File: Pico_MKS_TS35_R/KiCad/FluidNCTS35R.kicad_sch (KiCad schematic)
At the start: 8 parts, among them J1 Conn_01x03_Pin, J2 Conn_01x03_Pin, U1 Pico

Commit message: Add PCB
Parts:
- added C1, C2, C3: C_Polarized, Capacitor_SMD:C_1210_3225Metric_Pad1.33x2.70mm_HandSolder, symbol Device:C_Polarized
- J1: footprint Connector_JST:JST_SH_SM03B-SRSS-TB_1x03-1MP_P1.00mm_Horizontal -> Connector_PinSocket_2.54mm:PinSocket_1x03_P2.54mm_Horizontal
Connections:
- net +3V3: now also C1.1
- net +5V: now also C3.1
- net GND: now also C1.2, C2.2, C3.2
- net VDD: now reaches D1.1 (K), U1.39 (VSYS)
- net VDD: now also C2.1
- net SWCLK: now reaches J1.1 (Pin_1), U1.41 (SWCLK)
- net SWDIO: now reaches J1.3 (Pin_3), U1.43 (SWDIO)

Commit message: Add PCB and some button handlers
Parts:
- added TP1, TP10, TP11, TP12, TP13, TP14, TP15, TP16, TP2, TP3, TP4, TP5, TP6, TP7, TP8, TP9: TestPoint, TestPoint:TestPoint_Pad_D2.0mm, symbol Connector:TestPoint
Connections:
- net +3V3: now also TP12.1
- net +5V: now also TP14.1
- net BEEPER: now also TP6.1
- net GND: now also J2.2 (Pin_2), TP11.1, TP15.1, TP16.1; no longer J2.3 (Pin_3)
- net LCD_BACKLIGHT: now also TP7.1
- net LCD_CS: now also TP9.1
- net LCD_RESET: now also TP5.1
- net LCD_RS: now also TP4.1
- net MISO: now also TP10.1
- net MOSI: now also TP2.1
- net RESET: now also TP1.1
- net SCK: now also TP3.1
- net TOUCH_CS: now also TP8.1
- net VDD: now also TP13.1
- net RX: now reaches J2.1 (Pin_1)
- net RX: now also U1.2 (GPIO1); no longer U1.1 (GPIO0)
- new net TX: J2.3 (Pin_3), U1.1 (GPIO0)

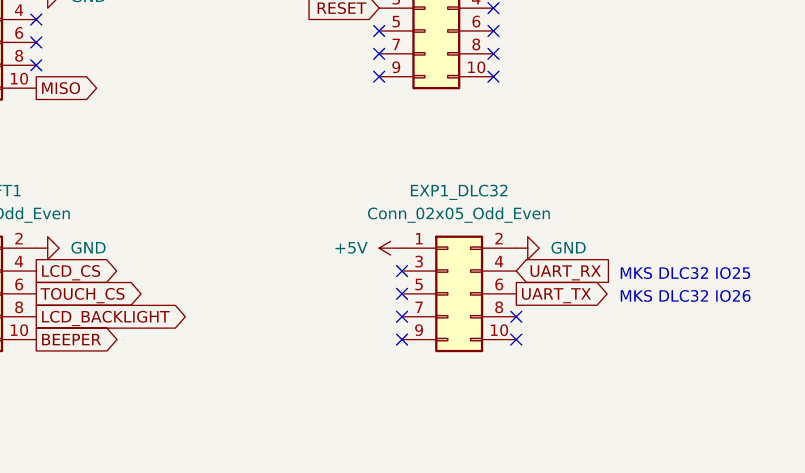
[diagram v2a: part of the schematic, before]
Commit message: Updated Board. Use GPIO 33 as input
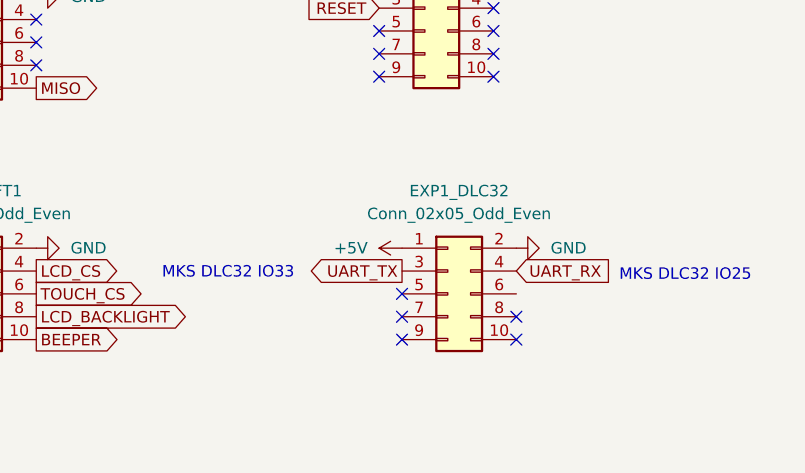
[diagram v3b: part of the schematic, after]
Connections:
- net UART_TX: now also EXP1_DLC32.3 (Pin_3); no longer EXP1_DLC32.6 (Pin_6)
- no-connect marks 36 -> 35
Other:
- note added: "MKS DLC32 IO33"
- note removed: "MKS DLC32 IO26"
- title: (none) -> FluidNC to MKS DLC32 Bridge
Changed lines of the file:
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@@
 	(generator_version "8.0")
 	(paper "A4")
+	(title_block
+		(title "FluidNC to MKS DLC32 Bridge")
+		(rev "3")
+	)
 	(junction
 		(at 168.91 110.49)
@@
 	(no_connect
 		(at 87.63 45.72)
-	)
-	(no_connect
-		(at 144.78 161.29)
 	)
 	(no_connect
@@
 		)
 	)
-	(text "MKS DLC32 IO26"
+	(text "MKS DLC32 IO33"
 		(exclude_from_sim no)
-		(at 168.91 165.1 0)
+		(at 118.11 162.306 0)
 		(effects
 			(font
@@
 	(global_label "UART_TX"
 		(shape output)
-		(at 157.48 163.83 0)
-		(fields_autoplaced yes)
-		(effects
-			(font
-				(size 1.27 1.27)
-			)
-			(justify left)
-		)
-		(property "Intersheetrefs" "${INTERSHEET_REFS}"
-			(at 168.2666 163.83 0)
-			(effects
-				(font
-					(size 1.27 1.27)
-				)
-				(justify left)
-				(hide yes)
-			)
+		(at 144.78 161.29 180)
+		(fields_autoplaced yes)
+		(effects
+			(font
+				(size 1.27 1.27)
+			)
+			(justify right)
+		)
+		(property "Intersheetrefs" "${INTERSHEET_REFS}"
+			(at 133.9934 161.29 0)
+			(effects
+				(font
+					(size 1.27 1.27)
+				)
+				(justify right)
+				(hide yes)
+			)
